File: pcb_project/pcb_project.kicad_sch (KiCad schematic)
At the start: 0 parts

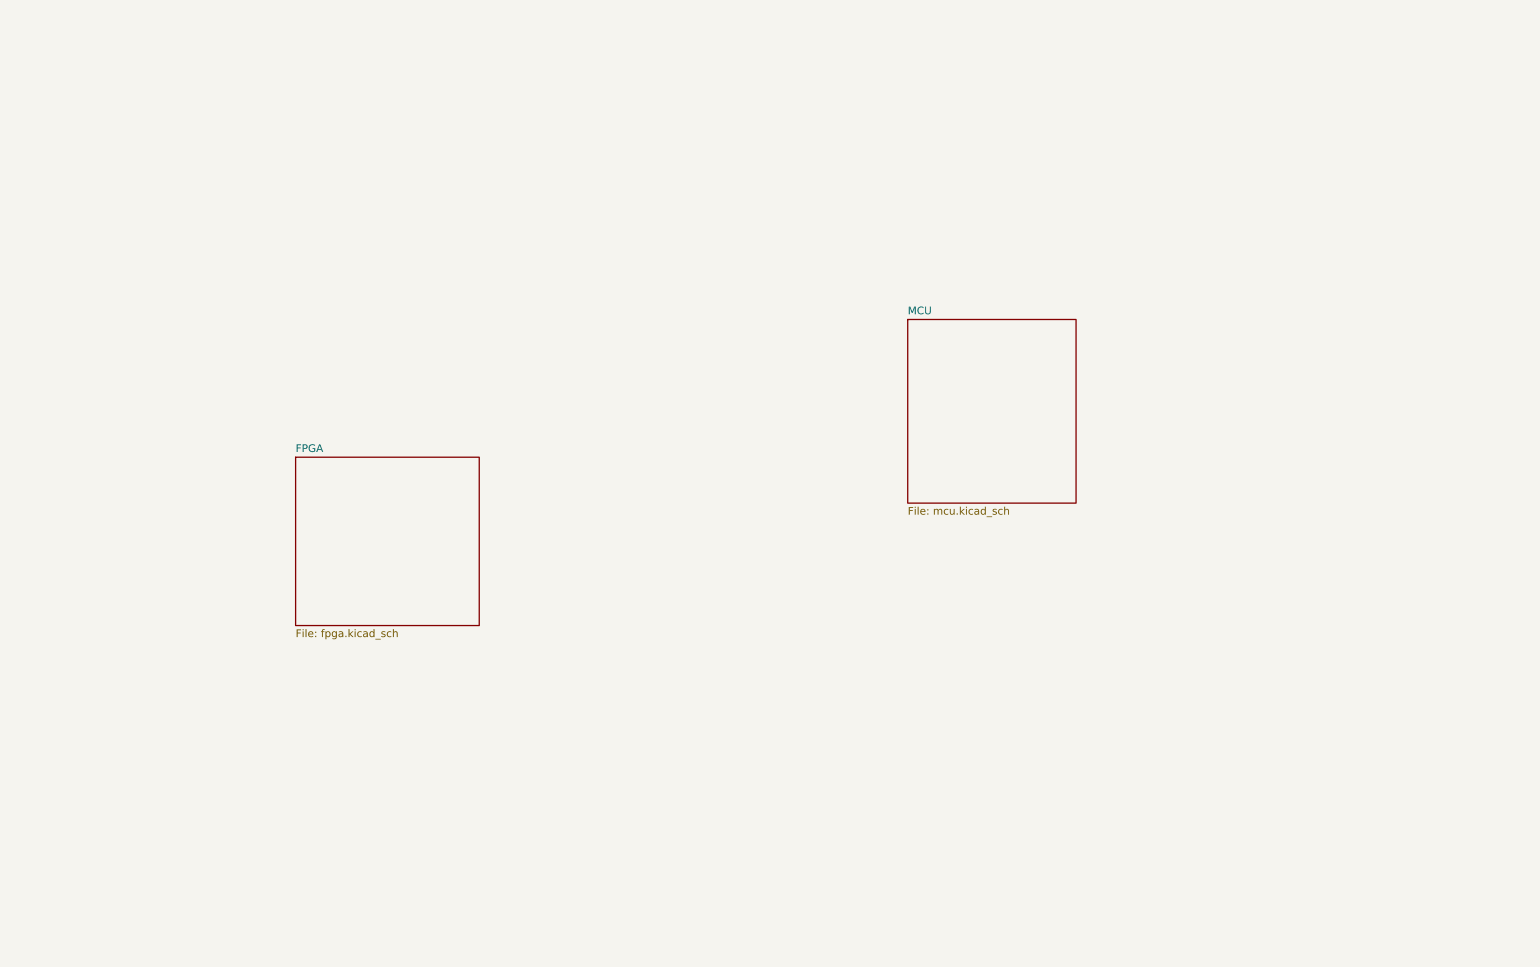
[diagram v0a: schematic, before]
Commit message: Add SD,VGA,Power modules
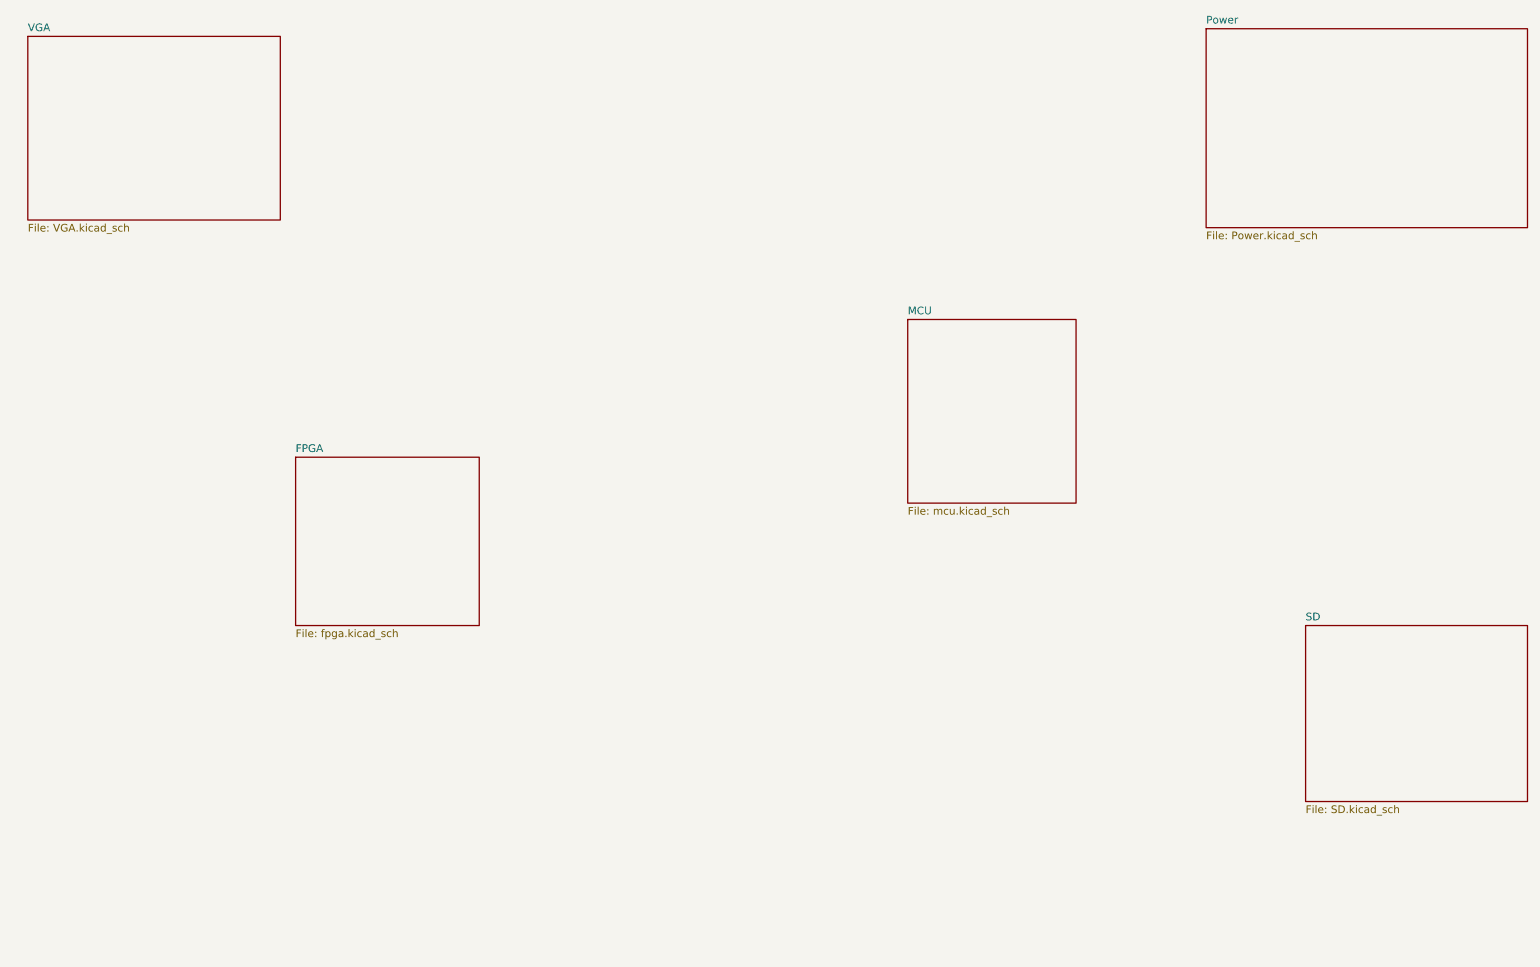
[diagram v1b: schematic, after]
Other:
- added sheet Power (Power.kicad_sch)
- added sheet SD (SD.kicad_sch)
- added sheet VGA (VGA.kicad_sch)
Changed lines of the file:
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@@
+		)
+	)
+	(sheet
+		(at 27.94 22.86)
+		(size 41.91 30.48)
+		(exclude_from_sim no)
+		(in_bom yes)
+		(on_board yes)
+		(dnp no)
+		(fields_autoplaced yes)
+		(stroke
+			(width 0.1524)
+			(type solid)
+		)
+		(fill
+			(color 0 0 0 0.0000)
+		)
+		(property "Sheetname" "VGA"
+			(at 27.94 22.1484 0)
+			(effects
+				(font
+					(size 1.27 1.27)
+				)
+				(justify left bottom)
+			)
+		)
+		(property "Sheetfile" "VGA.kicad_sch"
+			(at 27.94 53.9246 0)
+			(effects
+				(font
+					(size 1.27 1.27)
+				)
+				(justify left top)
+			)
+		)
+		(instances
+			(project "pcb_project"
+				(path "/98f80f66-4595-4d0f-90ca-59b2db6f447b"
+					(page "4")
+				)
+			)
+		)
+	)
+	(sheet
+		(at 223.52 21.59)
+		(size 53.34 33.02)
+		(exclude_from_sim no)
+		(in_bom yes)
+		(on_board yes)
+		(dnp no)
+		(fields_autoplaced yes)
+		(stroke
+			(width 0.1524)
+			(type solid)
+		)
+		(fill
+			(color 0 0 0 0.0000)
+		)
+		(property "Sheetname" "Power"
+			(at 223.52 20.8784 0)
+			(effects
+				(font
+					(size 1.27 1.27)
+				)
+				(justify left bottom)
+			)
+		)
+		(property "Sheetfile" "Power.kicad_sch"
+			(at 223.52 55.1946 0)
+			(effects
+				(font
+					(size 1.27 1.27)
+				)
+				(justify left top)
+			)
+		)
+		(instances
+			(project "pcb_project"
+				(path "/98f80f66-4595-4d0f-90ca-59b2db6f447b"
+					(page "5")
+				)
+			)
+		)
+	)
+	(sheet
+		(at 240.03 120.65)
+		(size 36.83 29.21)
+		(exclude_from_sim no)
+		(in_bom yes)
+		(on_board yes)
+		(dnp no)
+		(fields_autoplaced yes)
+		(stroke
+			(width 0.1524)
+			(type solid)
+		)
+		(fill
+			(color 0 0 0 0.0000)
+		)
+		(property "Sheetname" "SD"
+			(at 240.03 119.9384 0)
+			(effects
+				(font
+					(size 1.27 1.27)
+				)
+				(justify left bottom)
+			)
+		)
+		(property "Sheetfile" "SD.kicad_sch"
+			(at 240.03 150.4446 0)
+			(effects
+				(font
+					(size 1.27 1.27)
+				)
+				(justify left top)
+			)
+		)
+		(instances
+			(project "pcb_project"
+				(path "/98f80f66-4595-4d0f-90ca-59b2db6f447b"
+					(page "6")
+				)
+			)
 		)
 	)

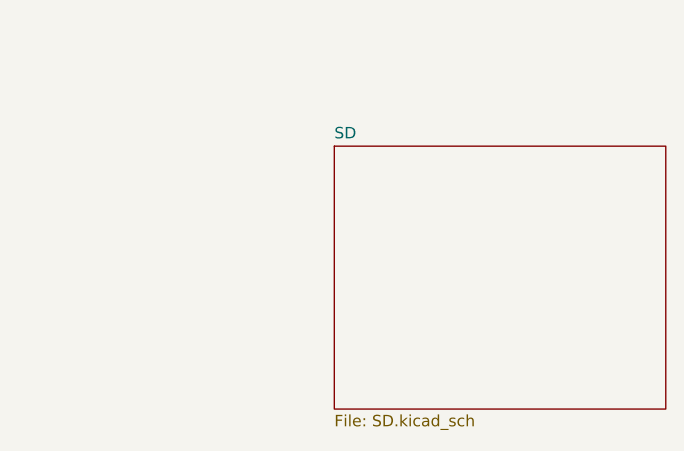
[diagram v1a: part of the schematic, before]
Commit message: Create MicroSD circuit
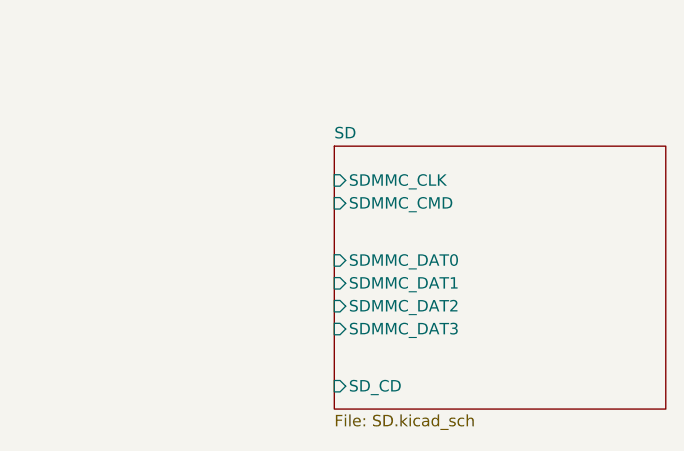
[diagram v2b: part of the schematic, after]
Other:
- sheet SD ports: added SDMMC_CLK, SDMMC_CMD, SDMMC_DAT0, SDMMC_DAT1, SDMMC_DAT2, SDMMC_DAT3, SD_CD; removed none
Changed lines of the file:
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@@
+			)
+		)
+		(pin "SDMMC_CLK" input
+			(at 240.03 124.46 180)
+			(effects
+				(font
+					(size 1.27 1.27)
+				)
+				(justify left)
+			)
+		)
+		(pin "SDMMC_CMD" input
+			(at 240.03 127 180)
+			(effects
+				(font
+					(size 1.27 1.27)
+				)
+				(justify left)
+			)
+		)
+		(pin "SDMMC_DAT0" input
+			(at 240.03 133.35 180)
+			(effects
+				(font
+					(size 1.27 1.27)
+				)
+				(justify left)
+			)
+		)
+		(pin "SDMMC_DAT1" input
+			(at 240.03 135.89 180)
+			(effects
+				(font
+					(size 1.27 1.27)
+				)
+				(justify left)
+			)
+		)
+		(pin "SDMMC_DAT2" input
+			(at 240.03 138.43 180)
+			(effects
+				(font
+					(size 1.27 1.27)
+				)
+				(justify left)
+			)
+		)
+		(pin "SDMMC_DAT3" input
+			(at 240.03 140.97 180)
+			(effects
+				(font
+					(size 1.27 1.27)
+				)
+				(justify left)
+			)
+		)
+		(pin "SD_CD" input
+			(at 240.03 147.32 180)
+			(effects
+				(font
+					(size 1.27 1.27)
+				)
+				(justify left)
 			)
 		)

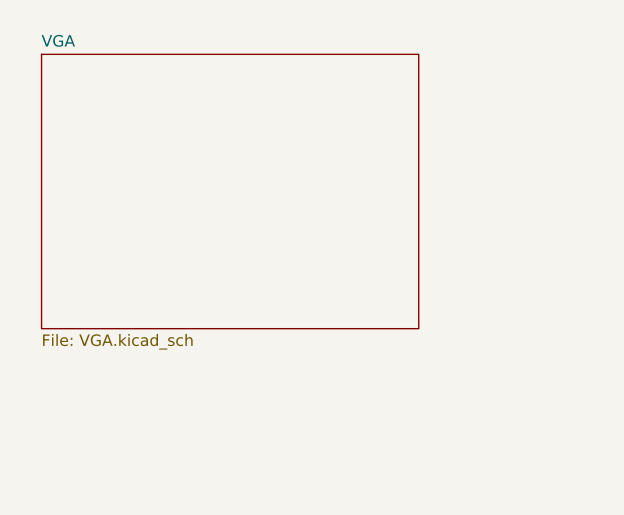
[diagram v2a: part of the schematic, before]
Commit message: Add VGA with 4bit DAC
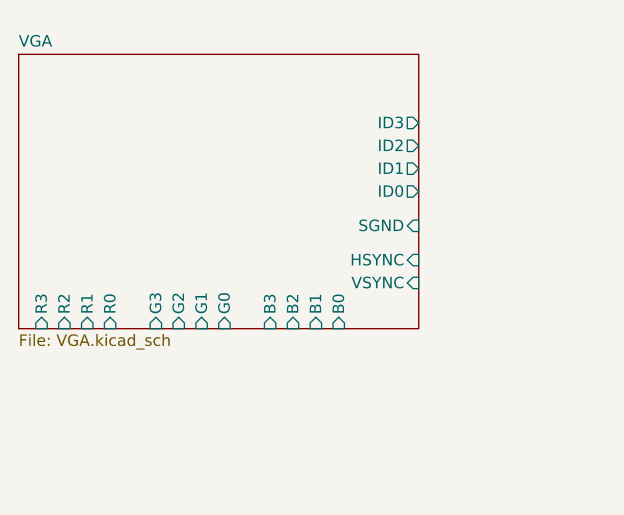
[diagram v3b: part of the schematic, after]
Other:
- sheet VGA ports: added B0, B1, B2, B3, G0, G1, G2, G3, HSYNC, ID0, ID1, ID2, ID3, R0, R1, R2, R3, SGND, VSYNC; removed none
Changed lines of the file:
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@@
 	)
 	(sheet
-		(at 27.94 22.86)
-		(size 41.91 30.48)
+		(at 25.4 22.86)
+		(size 44.45 30.48)
 		(exclude_from_sim no)
 		(in_bom yes)
@@
 		)
 		(property "Sheetname" "VGA"
-			(at 27.94 22.1484 0)
+			(at 25.4 22.1484 0)
 			(effects
 				(font
@@
 		)
 		(property "Sheetfile" "VGA.kicad_sch"
-			(at 27.94 53.9246 0)
+			(at 25.4 53.9246 0)
 			(effects
 				(font
@@
 			)
 		)
+		(pin "B0" input
+			(at 60.96 53.34 270)
+			(effects
+				(font
+					(size 1.27 1.27)
+				)
+				(justify left)
+			)
+		)
+		(pin "B2" input
+			(at 55.88 53.34 270)
+			(effects
+				(font
+					(size 1.27 1.27)
+				)
+				(justify left)
+			)
+		)
+		(pin "ID2" output
+			(at 69.85 33.02 0)
+			(effects
+				(font
+					(size 1.27 1.27)
+				)
+				(justify right)
+			)
+		)
+		(pin "HSYNC" input
+			(at 69.85 45.72 0)
+			(effects
+				(font
+					(size 1.27 1.27)
+				)
+				(justify right)
+			)
+		)
+		(pin "ID3" output
+			(at 69.85 30.48 0)
+			(effects
+				(font
+					(size 1.27 1.27)
+				)
+				(justify right)
+			)
+		)
+		(pin "ID1" output
+			(at 69.85 35.56 0)
+			(effects
+				(font
+					(size 1.27 1.27)
+				)
+				(justify right)
+			)
+		)
+		(pin "R3" input
+			(at 27.94 53.34 270)
+			(effects
+				(font
+					(size 1.27 1.27)
+				)
+				(justify left)
+			)
+		)
+		(pin "R0" input
+			(at 35.56 53.34 270)
+			(effects
+				(font
+					(size 1.27 1.27)
+				)
+				(justify left)
+			)
+		)
+		(pin "B3" input
+			(at 53.34 53.34 270)
+			(effects
+				(font
+					(size 1.27 1.27)
+				)
+				(justify left)
+			)
+		)
+		(pin "SGND" input
+			(at 69.85 41.91 0)
+			(effects
+				(font
+					(size 1.27 1.27)
+				)
+				(justify right)
+			)
+		)
+		(pin "G3" input
+			(at 40.64 53.34 270)
+			(effects
+				(font
+					(size 1.27 1.27)
+				)
+				(justify left)
+			)
+		)
+		(pin "G1" input
+			(at 45.72 53.34 270)
+			(effects
+				(font
+					(size 1.27 1.27)
+				)
+				(justify left)
+			)
+		)
+		(pin "G2" input
+			(at 43.18 53.34 270)
+			(effects
+				(font
+					(size 1.27 1.27)
+				)
+				(justify left)
+			)
+		)
+		(pin "ID0" output
+			(at 69.85 38.1 0)
+			(effects
+				(font
+					(size 1.27 1.27)
+				)
+				(justify right)
+			)
+		)
+		(pin "R1" input
+			(at 33.02 53.34 270)
+			(effects
+				(font
+					(size 1.27 1.27)
+				)
+				(justify left)
+			)
+		)
+		(pin "R2" input
+			(at 30.48 53.34 270)
+			(effects
+				(font
+					(size 1.27 1.27)
+				)
+				(justify left)
+			)
+		)
+		(pin "G0" input
+			(at 48.26 53.34 270)
+			(effects
+				(font
+					(size 1.27 1.27)
+				)
+				(justify left)
+			)
+		)
+		(pin "VSYNC" input
+			(at 69.85 48.26 0)
+			(effects
+				(font
+					(size 1.27 1.27)
+				)
+				(justify right)
+			)
+		)
+		(pin "B1" input
+			(at 58.42 53.34 270)
+			(effects
+				(font
+					(size 1.27 1.27)
+				)
+				(justify left)
+			)
+		)

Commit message: Add USB (have questions)
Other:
- added sheet USB (USB.kicad_sch)
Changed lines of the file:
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@@
+	)
+	(sheet
+		(at 162.56 26.67)
+		(size 29.21 17.78)
+		(exclude_from_sim no)
+		(in_bom yes)
+		(on_board yes)
+		(dnp no)
+		(fields_autoplaced yes)
+		(stroke
+			(width 0.1524)
+			(type solid)
+		)
+		(fill
+			(color 0 0 0 0.0000)
+		)
+		(property "Sheetname" "USB"
+			(at 162.56 25.9584 0)
+			(effects
+				(font
+					(size 1.27 1.27)
+				)
+				(justify left bottom)
+			)
+		)
+		(property "Sheetfile" "USB.kicad_sch"
+			(at 162.56 45.0346 0)
+			(effects
+				(font
+					(size 1.27 1.27)
+				)
+				(justify left top)
+			)
+		)
+		(pin "PSU_+5V" input
+			(at 191.77 33.02 0)
+			(effects
+				(font
+					(size 1.27 1.27)
+				)
+				(justify right)
+			)
+		)
+		(pin "USB_ID" input
+			(at 186.69 44.45 270)
+			(effects
+				(font
+					(size 1.27 1.27)
+				)
+				(justify left)
+			)
+		)
+		(pin "PSU_+3.3V" input
+			(at 191.77 29.21 0)
+			(effects
+				(font
+					(size 1.27 1.27)
+				)
+				(justify right)
+			)
+		)
+		(pin "D+" input
+			(at 179.07 44.45 270)
+			(effects
+				(font
+					(size 1.27 1.27)
+				)
+				(justify left)
+			)
+		)
+		(pin "USB_MCU_EN" input
+			(at 171.45 44.45 270)
+			(effects
+				(font
+					(size 1.27 1.27)
+				)
+				(justify left)
+			)
+		)
+		(pin "MCU_USB_OC" input
+			(at 167.64 44.45 270)
+			(effects
+				(font
+					(size 1.27 1.27)
+				)
+				(justify left)
+			)
+		)
+		(pin "D-" input
+			(at 182.88 44.45 270)
+			(effects
+				(font
+					(size 1.27 1.27)
+				)
+				(justify left)
+			)
+		)
+		(instances
+			(project "pcb_project"
+				(path "/98f80f66-4595-4d0f-90ca-59b2db6f447b"
+					(page "7")
+				)
+			)
+		)
 	)
 	(sheet

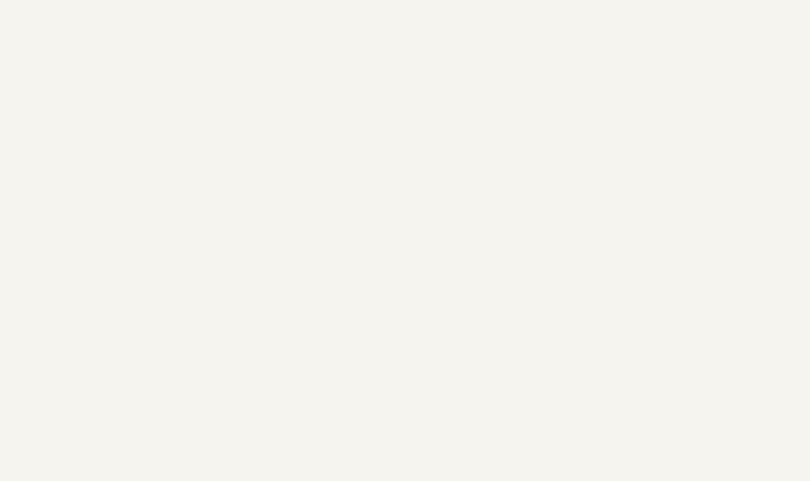
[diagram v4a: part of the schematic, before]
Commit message: Actuall controller joystick schematic
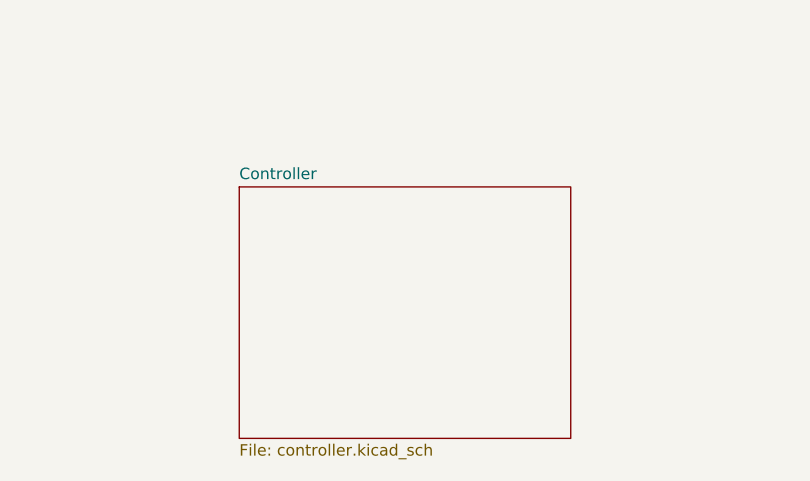
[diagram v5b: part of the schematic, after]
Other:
- added sheet Controller (controller.kicad_sch)
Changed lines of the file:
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@@
+	)
+	(sheet
+		(at 125.73 144.78)
+		(size 36.83 27.94)
+		(exclude_from_sim no)
+		(in_bom yes)
+		(on_board yes)
+		(dnp no)
+		(fields_autoplaced yes)
+		(stroke
+			(width 0.1524)
+			(type solid)
+		)
+		(fill
+			(color 0 0 0 0.0000)
+		)
+		(property "Sheetname" "Controller"
+			(at 125.73 144.0684 0)
+			(effects
+				(font
+					(size 1.27 1.27)
+				)
+				(justify left bottom)
+			)
+		)
+		(property "Sheetfile" "controller.kicad_sch"
+			(at 125.73 173.3046 0)
+			(effects
+				(font
+					(size 1.27 1.27)
+				)
+				(justify left top)
+			)
+		)
+		(instances
+			(project "pcb_project"
+				(path "/98f80f66-4595-4d0f-90ca-59b2db6f447b"
+					(page "8")
+				)
+			)
+		)
 	)
 	(sheet

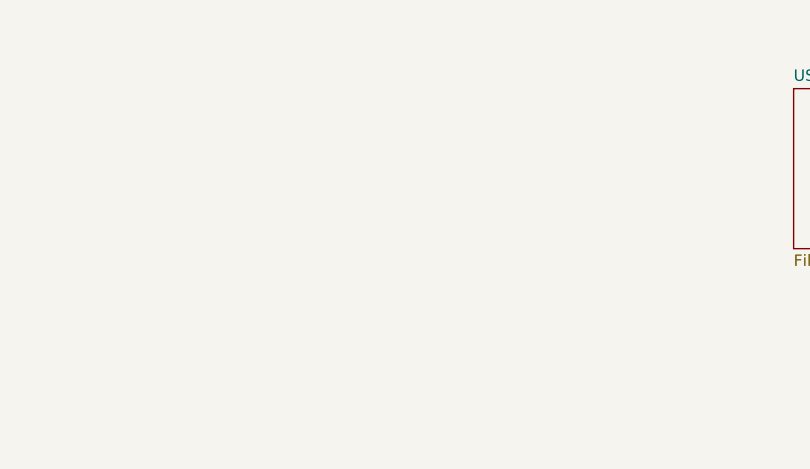
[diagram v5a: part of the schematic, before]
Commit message: Add symbolforLED
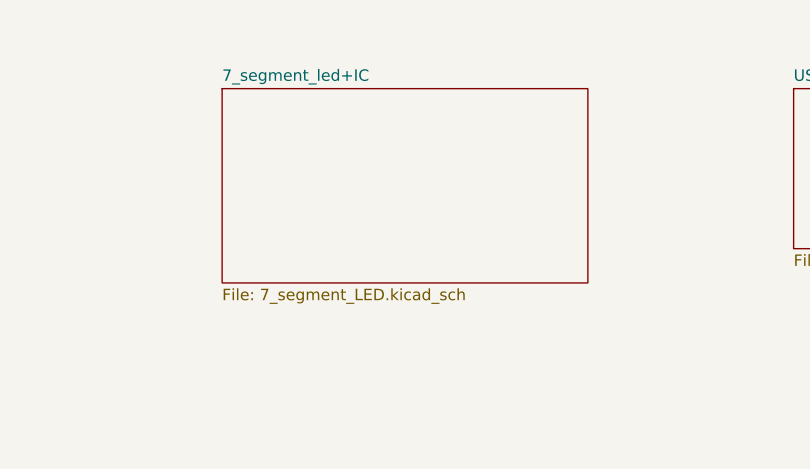
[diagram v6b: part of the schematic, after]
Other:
- added sheet 7_segment_led+IC (7_segment_LED.kicad_sch)
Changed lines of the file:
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@@
+	)
+	(sheet
+		(at 99.06 26.67)
+		(size 40.64 21.59)
+		(exclude_from_sim no)
+		(in_bom yes)
+		(on_board yes)
+		(dnp no)
+		(fields_autoplaced yes)
+		(stroke
+			(width 0.1524)
+			(type solid)
+		)
+		(fill
+			(color 0 0 0 0.0000)
+		)
+		(property "Sheetname" "7_segment_led+IC"
+			(at 99.06 25.9584 0)
+			(effects
+				(font
+					(size 1.27 1.27)
+				)
+				(justify left bottom)
+			)
+		)
+		(property "Sheetfile" "7_segment_LED.kicad_sch"
+			(at 99.06 48.8446 0)
+			(effects
+				(font
+					(size 1.27 1.27)
+				)
+				(justify left top)
+			)
+		)
+		(instances
+			(project "pcb_project"
+				(path "/98f80f66-4595-4d0f-90ca-59b2db6f447b"
+					(page "9")
+				)
+			)
+		)
 	)
 	(sheet
